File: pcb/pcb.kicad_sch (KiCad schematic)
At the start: 6 parts, among them J1 vik-module-connector, J2 Conn_01x05_Socket

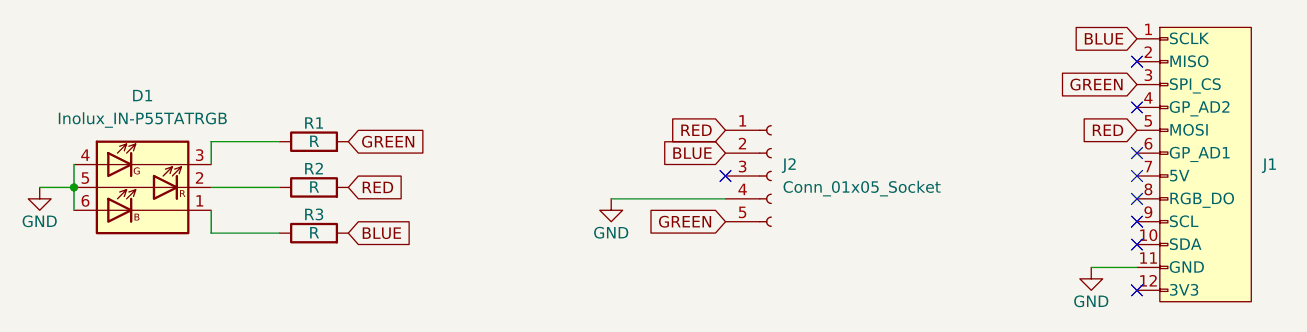
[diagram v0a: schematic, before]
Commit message: support VIK adapter
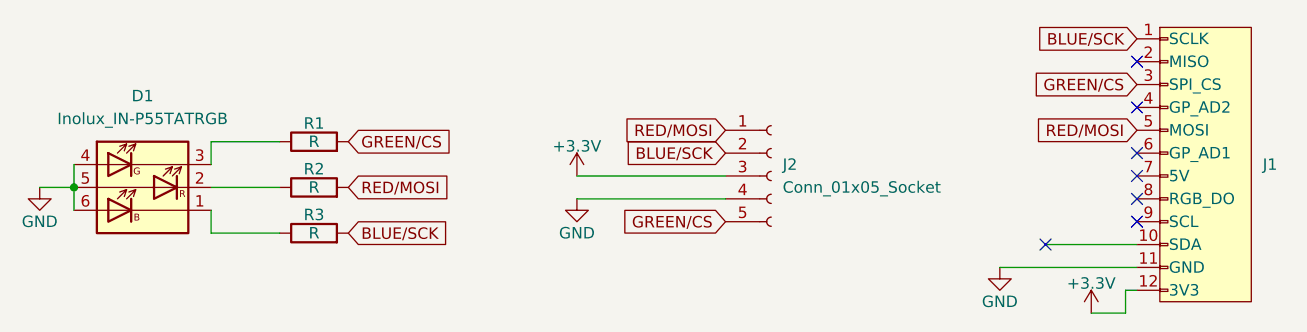
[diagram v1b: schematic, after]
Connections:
- net +3.3V: now reaches J1.12 (3V3)
- net +3.3V: now also J2.3 (Pin_3)
- net BLUE renamed BLUE/SCK
- net GREEN renamed GREEN/CS
- net RED renamed RED/MOSI
- no-connect marks 9 -> 7
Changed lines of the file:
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@@
-	)
-	(no_connect
-		(at 149.86 50.8)
-	)
-	(no_connect
-		(at 104.14 38.1)
 	)
 	(no_connect
@@
 	)
 	(no_connect
-		(at 149.86 45.72)
+		(at 139.7 45.72)
 	)
 	(no_connect
@@
 	(wire
 		(pts
+			(xy 139.7 45.72) (xy 149.86 45.72)
+		)
+		(stroke
+			(width 0)
+			(type default)
+		)
+	)
+	(wire
+		(pts
 			(xy 46.99 39.37) (xy 54.61 39.37)
 		)
@@
 	(wire
 		(pts
-			(xy 144.78 48.26) (xy 149.86 48.26)
+			(xy 148.59 50.8) (xy 149.86 50.8)
+		)
+		(stroke
+			(width 0)
+			(type default)
+		)
+	)
+	(wire
+		(pts
+			(xy 134.62 48.26) (xy 149.86 48.26)
 		)
 		(stroke
@@
 	(wire
 		(pts
-			(xy 91.44 40.64) (xy 104.14 40.64)
+			(xy 87.63 40.64) (xy 104.14 40.64)
+		)
+		(stroke
+			(width 0)
+			(type default)
+		)
+	)
+	(wire
+		(pts
+			(xy 148.59 53.34) (xy 148.59 50.8)
+		)
+		(stroke
+			(width 0)
+			(type default)
+		)
+	)
+	(wire
+		(pts
+			(xy 144.78 53.34) (xy 148.59 53.34)
+		)
+		(stroke
+			(width 0)
+			(type default)
+		)
+	)
+	(wire
+		(pts
+			(xy 87.63 38.1) (xy 104.14 38.1)
 		)
 		(stroke
@@
 		)
 	)
-	(global_label "BLUE"
+	(global_label "BLUE/SCK"
 		(shape input)
 		(at 62.23 44.45 0)
@@
 		)
 	)
-	(global_label "RED"
+	(global_label "RED{slash}MOSI"
 		(shape input)
 		(at 62.23 39.37 0)
@@
 		)
 		(property "Intersheetrefs" "${INTERSHEET_REFS}"
-			(at 68.9042 39.37 0)
+			(at 74.8309 39.37 0)
 			(effects
 				(font
@@
 		)
 	)
-	(global_label "BLUE"
+	(global_label "BLUE/SCK"
 		(shape input)
 		(at 149.86 22.86 180)
@@
 		)
 	)
-	(global_label "BLUE"
+	(global_label "BLUE/SCK"
 		(shape input)
 		(at 104.14 35.56 180)
@@
 		)
 		(property "Intersheetrefs" "${INTERSHEET_REFS}"
-			(at 96.3772 35.56 0)
+			(at 91.2972 35.56 0)
 			(effects
 				(font
@@
 		)
 	)
-	(global_label "GREEN"
+	(global_label "GREEN/CS"
 		(shape input)
 		(at 104.14 43.18 180)
@@
 		)
 	)
-	(global_label "GREEN"
+	(global_label "GREEN/CS"
 		(shape input)
 		(at 149.86 27.94 180)
@@
 		)
 	)
-	(global_label "RED"
+	(global_label "RED{slash}MOSI"
 		(shape input)
 		(at 149.86 33.02 180)
@@
 		)
 		(property "Intersheetrefs" "${INTERSHEET_REFS}"
-			(at 143.1858 33.02 0)
+			(at 137.2591 33.02 0)
 			(effects
 				(font
@@
 		)
 	)
-	(global_label "GREEN"
+	(global_label "GREEN/CS"
 		(shape input)
 		(at 62.23 34.29 0)
@@
 		)
 	)
-	(global_label "RED"
+	(global_label "RED{slash}MOSI"
 		(shape input)
 		(at 104.14 33.02 180)
@@
 		)
 		(property "Intersheetrefs" "${INTERSHEET_REFS}"
-			(at 97.4658 33.02 0)
+			(at 91.5391 33.02 0)
 			(effects
 				(font
@@
 	(symbol
 		(lib_id "power:GND")
-		(at 144.78 48.26 0)
+		(at 134.62 48.26 0)
 		(unit 1)
 		(exclude_from_sim no)
@@
 		(dnp no)
 		(property "Reference" "#PWR03"
-			(at 144.78 54.61 0)
+			(at 134.62 54.61 0)
 			(effects
 				(font
@@
 		)
 		(property "Value" "GND"
-			(at 144.78 52.07 0)
+			(at 134.62 52.07 0)
 			(effects
 				(font
@@
 		)
 		(property "Footprint" ""
-			(at 144.78 48.26 0)
+			(at 134.62 48.26 0)
 			(effects
 				(font
@@
 		)
 		(property "Datasheet" ""
-			(at 144.78 48.26 0)
+			(at 134.62 48.26 0)
 			(effects
 				(font
@@
 		)
 		(property "Description" ""
-			(at 144.78 48.26 0)
+			(at 134.62 48.26 0)
 			(effects
 				(font
@@
 	)
 	(symbol
+		(lib_id "power:+3.3V")
+		(at 144.78 53.34 0)
+		(unit 1)
+		(exclude_from_sim no)
+		(in_bom yes)
+		(on_board yes)
+		(dnp no)
+		(property "Reference" "#PWR04"
+			(at 144.78 57.15 0)
+			(effects
+				(font
+					(size 1.27 1.27)
+				)
+				(hide yes)
+			)
+		)
+		(property "Value" "+3.3V"
+			(at 144.78 50.038 0)
+			(effects
+				(font
+					(size 1.27 1.27)
+				)
+			)
+		)
+		(property "Footprint" ""
+			(at 144.78 53.34 0)
+			(effects
+				(font
+					(size 1.27 1.27)
+				)
+				(hide yes)
+			)
+		)
+		(property "Datasheet" ""
+			(at 144.78 53.34 0)
+			(effects
+				(font
+					(size 1.27 1.27)
+				)
+				(hide yes)
+			)
+		)
+		(property "Description" "Power symbol creates a global label with name \"+3.3V\""
+			(at 144.78 53.34 0)
+			(effects
+				(font
+					(size 1.27 1.27)
+				)
+				(hide yes)
+			)
+		)
+		(pin "1"
+		)
+		(instances
+			(project "pcb"
+				(path "/82610637-5aef-44b0-8401-942b82c77267"
+					(reference "#PWR04")
+					(unit 1)
+				)
+			)
+		)
+	)
+	(symbol
 		(lib_id "power:GND")
 		(at 27.94 39.37 0)
@@
 	(symbol
 		(lib_id "power:GND")
-		(at 91.44 40.64 0)
+		(at 87.63 40.64 0)
 		(unit 1)
 		(exclude_from_sim no)
@@
 		(dnp no)
 		(property "Reference" "#PWR02"
-			(at 91.44 46.99 0)
+			(at 87.63 46.99 0)
 			(effects
 				(font
@@
 		)
 		(property "Value" "GND"
-			(at 91.44 44.45 0)
+			(at 87.63 44.45 0)
 			(effects
 				(font
@@
 		)
 		(property "Footprint" ""
-			(at 91.44 40.64 0)
+			(at 87.63 40.64 0)
 			(effects
 				(font
@@
 		)
 		(property "Datasheet" ""
-			(at 91.44 40.64 0)
+			(at 87.63 40.64 0)
 			(effects
 				(font
@@
 		)
 		(property "Description" ""
-			(at 91.44 40.64 0)
+			(at 87.63 40.64 0)
 			(effects
 				(font
@@
 					(unit 1)
 				)
+			)
+		)
+	)
+	(symbol
+		(lib_id "power:+3.3V")
+		(at 87.63 38.1 0)
+		(unit 1)
+		(exclude_from_sim no)
+		(in_bom yes)
+		(on_board yes)
+		(dnp no)
+		(property "Reference" "#PWR05"
+			(at 87.63 41.91 0)
+			(effects
+				(font
+					(size 1.27 1.27)
+				)
+				(hide yes)
+			)
+		)
+		(property "Value" "+3.3V"
+			(at 87.63 34.798 0)
+			(effects
+				(font
+					(size 1.27 1.27)
+				)
+			)
+		)
+		(property "Footprint" ""
+			(at 87.63 38.1 0)
+			(effects
+				(font
+					(size 1.27 1.27)
+				)
+				(hide yes)
+			)
+		)
+		(property "Datasheet" ""
+			(at 87.63 38.1 0)
+			(effects
+				(font
+					(size 1.27 1.27)
+				)
+				(hide yes)
+			)
+		)
+		(property "Description" "Power symbol creates a global label with name \"+3.3V\""
+			(at 87.63 38.1 0)
+			(effects
+				(font
+					(size 1.27 1.27)
+				)
+				(hide yes)
+			)
+		)
+		(pin "1"
+		)
+		(instances
+			(project ""
+				(path "/82610637-5aef-44b0-8401-942b82c77267"
+					(reference "#PWR05")
+					(unit 1)
+				)
